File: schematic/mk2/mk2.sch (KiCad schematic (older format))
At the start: 0 parts

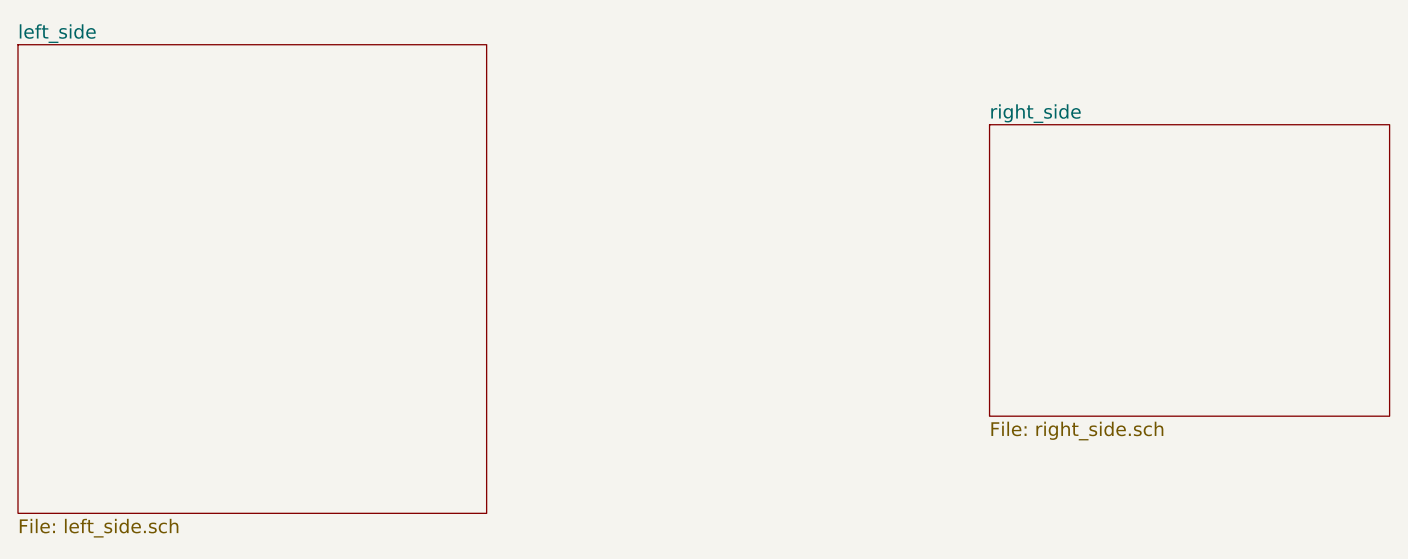
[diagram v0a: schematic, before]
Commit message: schematic: Fix the hierarchical schematics and add outputs to left_side
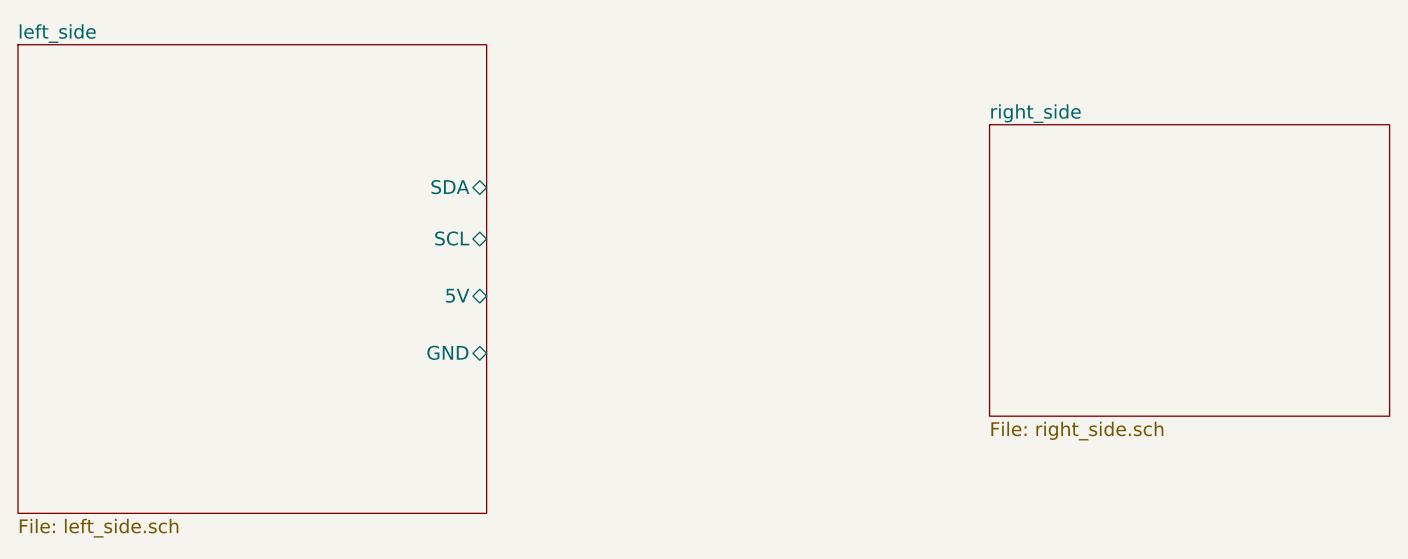
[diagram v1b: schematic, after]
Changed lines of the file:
@@
 EESchema Schematic File Version 2
+LIBS:arduino
 LIBS:power
 LIBS:device
@@
 LIBS:contrib
 LIBS:valves
+LIBS:mylib_experimental
+LIBS:rur
+LIBS:mk2-cache
 EELAYER 25 0
 EELAYER END
@@
 F0 "left_side" 60
 F1 "left_side.sch" 60
+F2 "SDA" B R 5075 2625 60
+F3 "SCL" B R 5075 2850 60
+F4 "5V" B R 5075 3100 60
+F5 "GND" B R 5075 3350 60
 $EndSheet
 $Sheet
